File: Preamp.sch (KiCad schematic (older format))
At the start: 107 parts, among them J10 RCAJack, J11 XLR4BODYPIN, J12 XLR4BODYPIN, J13 XLR4BODYPIN, J4 RCAJack, J5 RCAJack, SW1 SW_SPST, U3 LM4562, U4 LM4562, U5 LM4562, U6 LM4562, U7 THAT1646, U8 THAT1646, U9 THAT1646

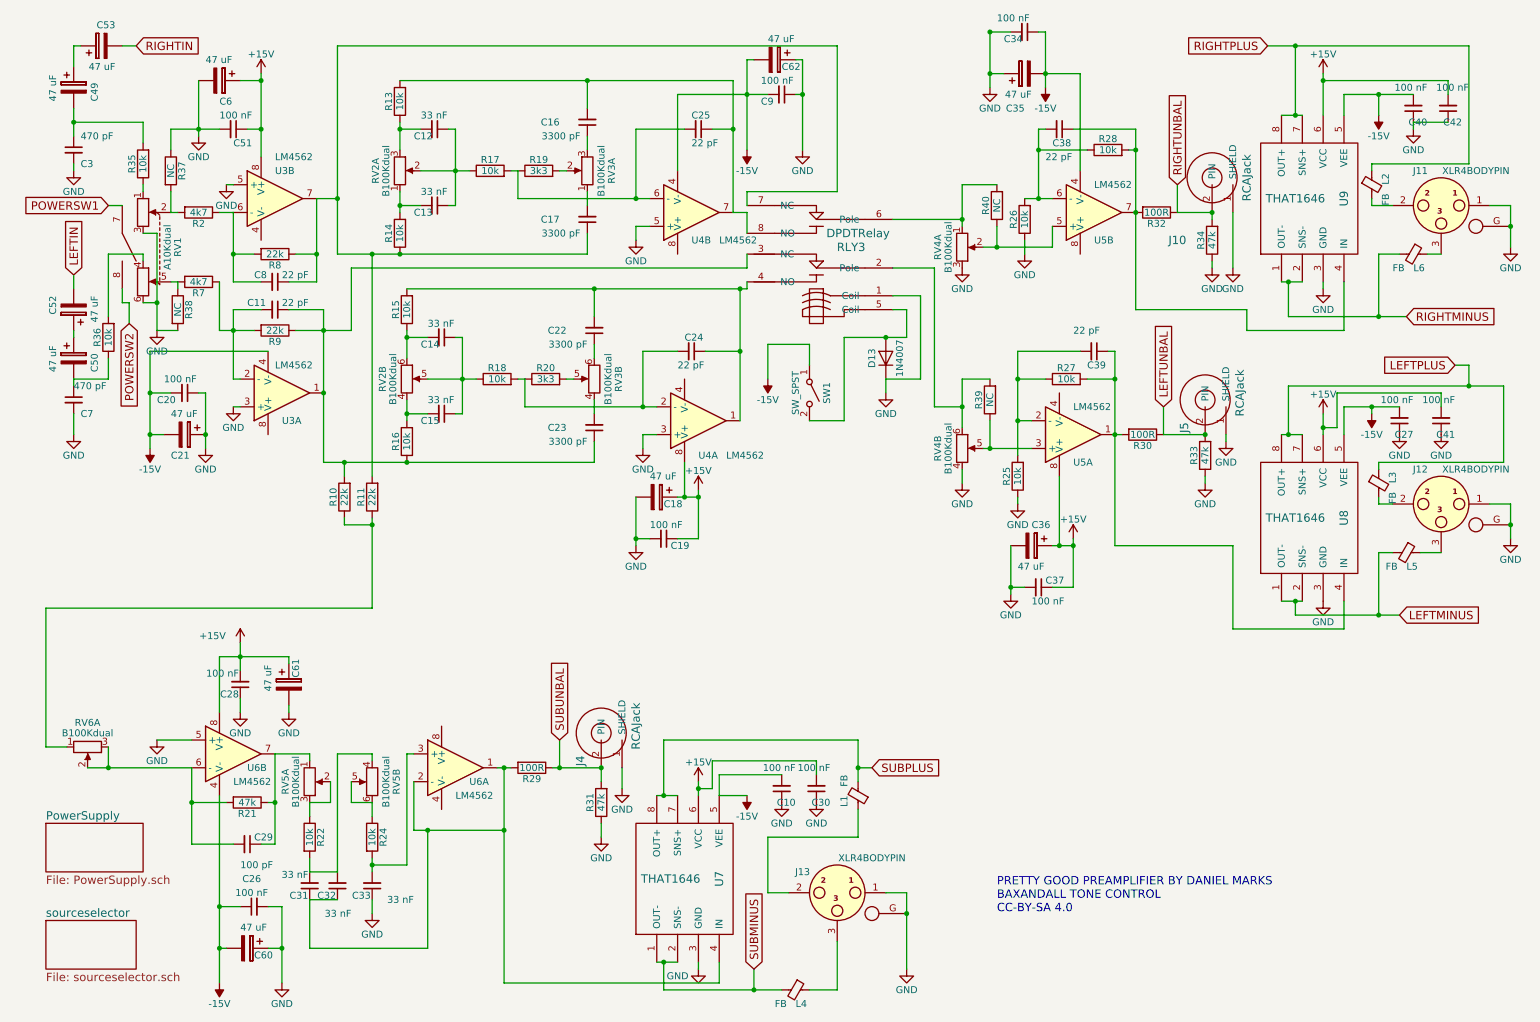
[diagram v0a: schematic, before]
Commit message: Added jumpers to connect shields of XLR to ground
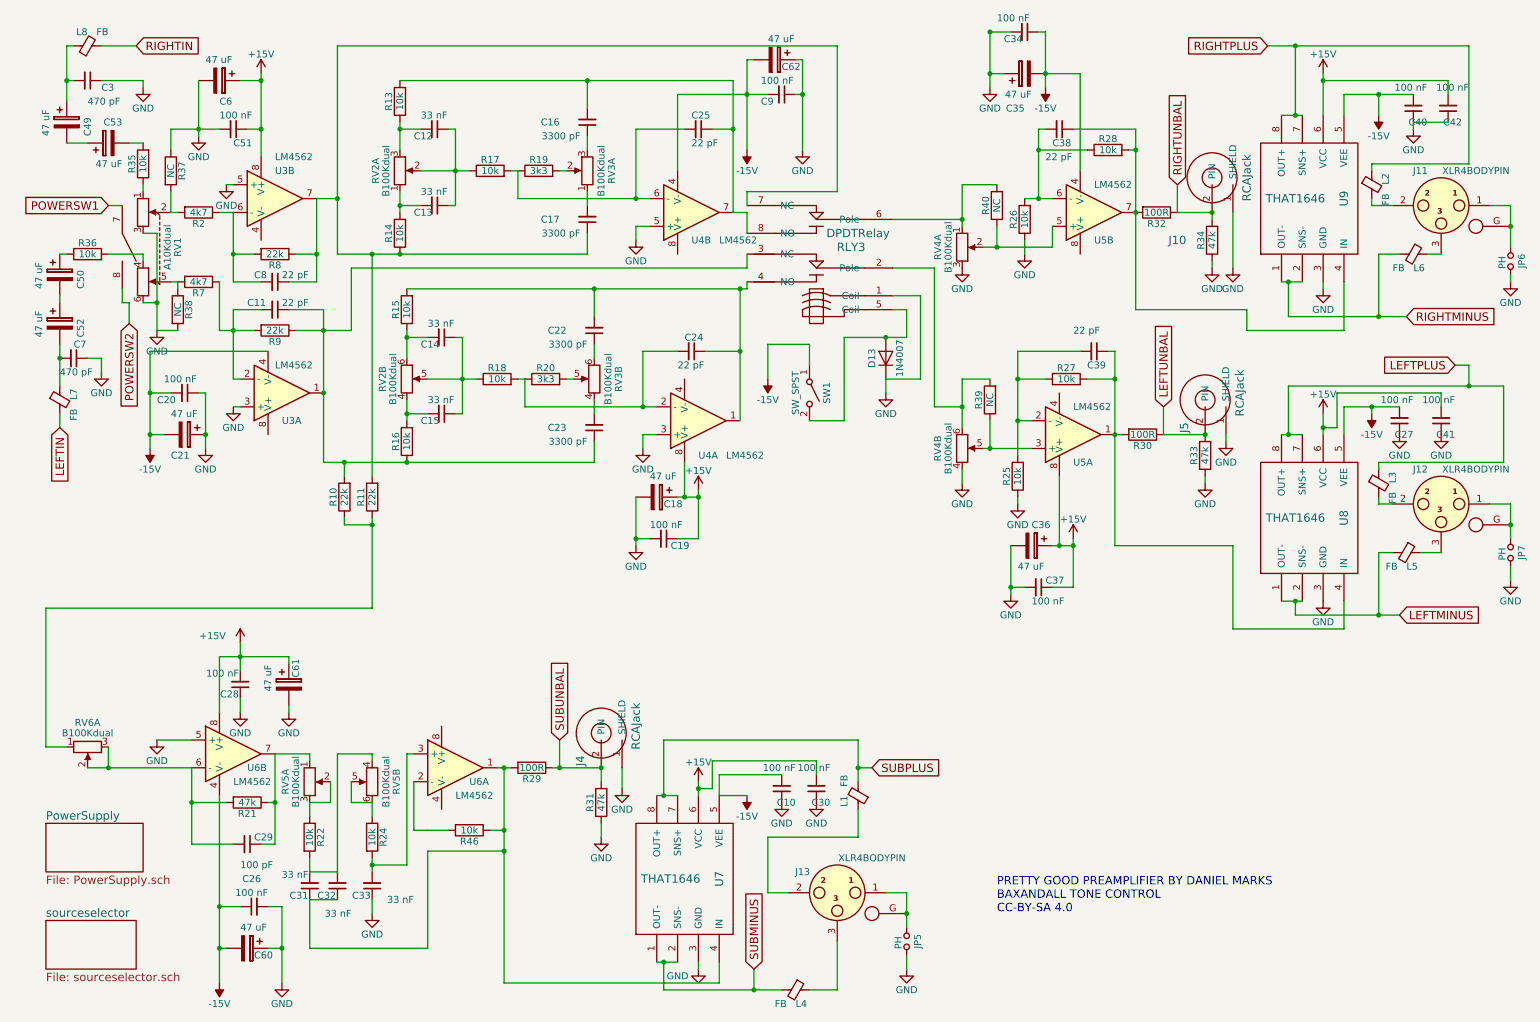
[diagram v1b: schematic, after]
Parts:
- added JP5, JP6, JP7: PH, Pin_Headers:Pin_Header_Straight_1x02_Pitch2.54mm, symbol Jumper_NO_Small
- added L7, L8: FB, Inductors_THT:L_Axial_L7.0mm_D3.3mm_P10.16mm_Horizontal_Fastron_MICC, symbol Ferrite_Bead_Small
- added R46: 10k, Resistors_THT:R_Axial_DIN0207_L6.3mm_D2.5mm_P7.62mm_Horizontal, symbol R
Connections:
- net GND: now also C3.1, JP5.2, JP6.2, JP7.2; no longer C3.2, C7.2, J11.1, J11.G, J12.1, J12.G, J13.1, J13.G
- net LEFTIN: now also L7.2; no longer C52.2
- net RIGHTIN: now also L8.2; no longer C53.2
- net at C31.1, C32.1, R29.2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: now also R46.1; no longer U6.2 (-)
- net at C53.1: now also C49.2; no longer C49.1
- net at C50.1: now also R36.1; no longer C52.1
- new net: C52.2, C7.2, L7.1
- new net: C53.2, R35.2
- new net: C50.2, C52.1
- new net: C3.2, C49.1, L8.1
- new net: R46.2, U6.2 (-)
- new net: J12.1, J12.G, JP7.1
- new net: J11.1, J11.G, JP6.1
- new net: J13.1, J13.G, JP5.1
- now unconnected: C7.1
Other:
- moved on the sheet: C49, C50, C52, C53, C7, R36

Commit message: JLCPCB manufacturing
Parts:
- added C66, C67, C68, C69, C70, C71: 47 uF, Capacitors_THT:CP_Radial_D5.0mm_P2.50mm, symbol CP
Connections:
- net LEFTUNBAL: now also C69.1; no longer R30.1
- net RIGHTUNBAL: now also C71.1; no longer R32.1
- net SUBUNBAL: now also C67.1; no longer R29.1
- net at C7.2, L7.1: now also C52.1; no longer C52.2
- net at C31.1, C32.1, R46.1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: now also R29.1; no longer R29.2
- net at R35.2: now also C53.1; no longer C53.2
- net at C39.1, R27.2, U5.1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: now also R30.1; no longer R30.2
- net at C49.2: now also C53.2; no longer C53.1
- net at C50.2: now also C52.2; no longer C52.1
- new net: C66.1, R29.2
- new net: C70.1, R32.1
- new net: C68.1, R30.2
- new net: C70.2, C71.2
- new net: C68.2, C69.2
- new net: C66.2, C67.2
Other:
- moved on the sheet: J5, R29, R30, R32, R33

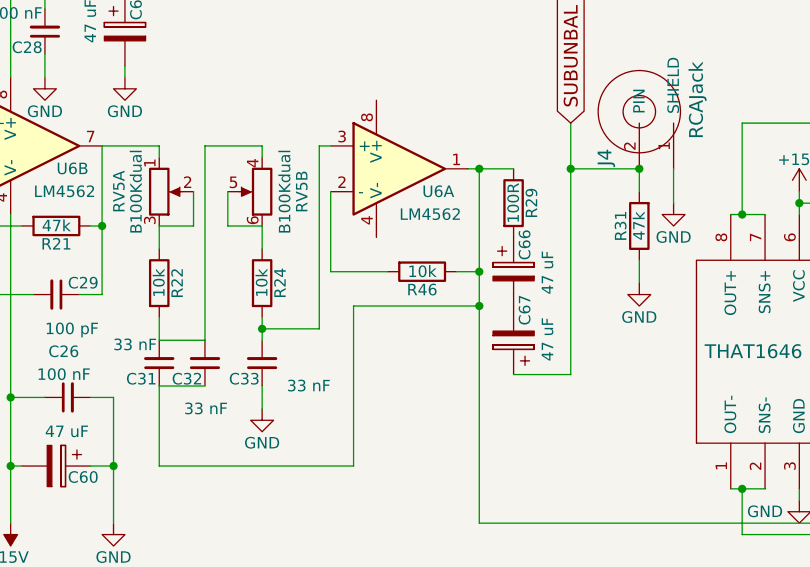
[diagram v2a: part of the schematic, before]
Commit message: A few minor changes to fix crowding of components
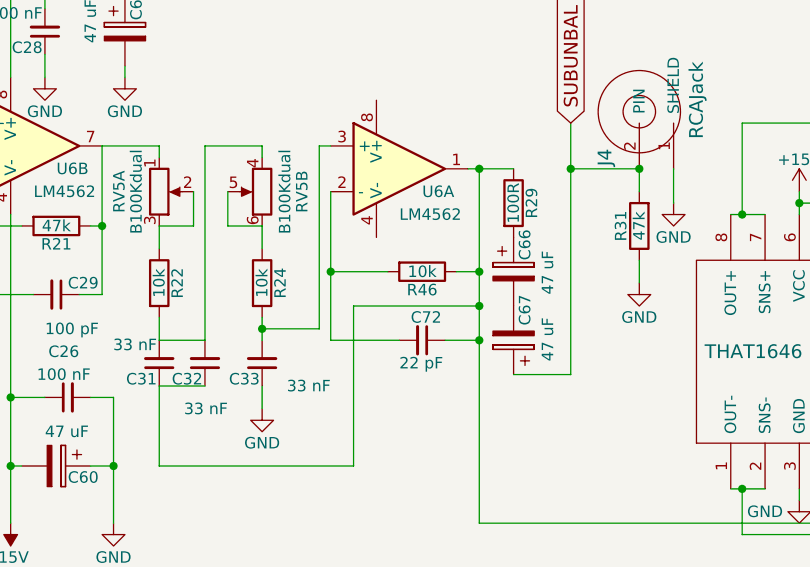
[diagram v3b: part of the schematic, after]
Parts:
- added C72: 22 pF, Capacitors_THT:C_Disc_D5.0mm_W2.5mm_P5.00mm, symbol C_Small
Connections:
- net at C31.1, C32.1, R29.1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: now also C72.1
- net at R46.2, U6.2 (-): now also C72.2
